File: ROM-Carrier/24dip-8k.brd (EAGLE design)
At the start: 33 x 26.7 mm, 7 parts

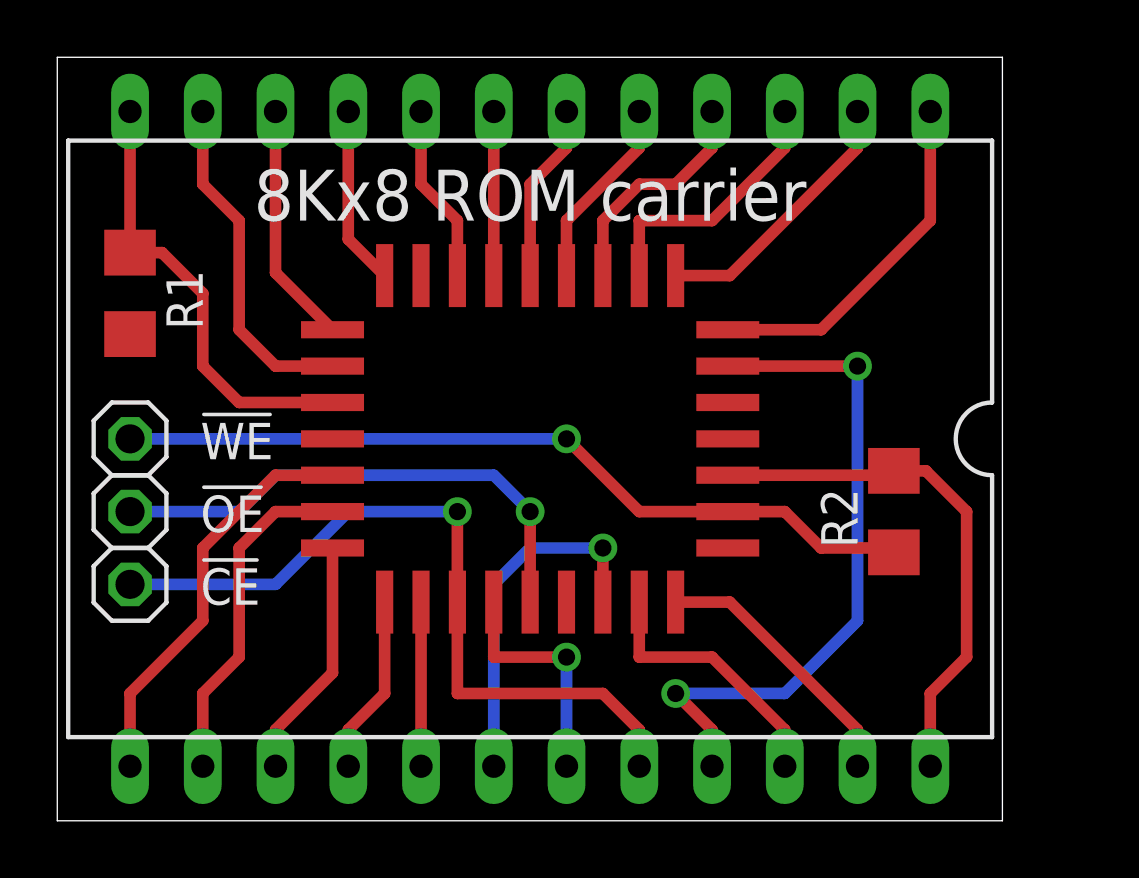
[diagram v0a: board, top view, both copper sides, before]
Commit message: fix carrier board (was 24-9, needed to be 24-6) removed unnecessary z80 support from 8080 sim
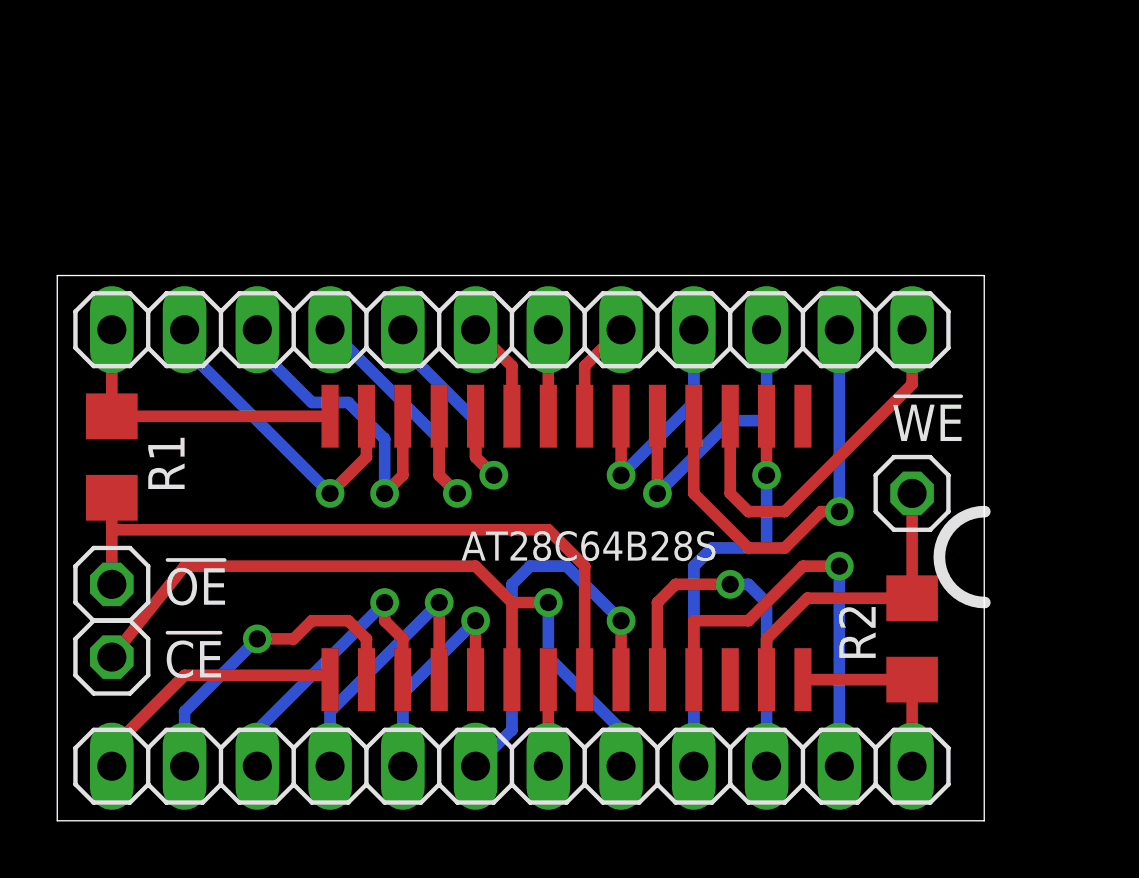
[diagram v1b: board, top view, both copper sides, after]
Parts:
- removed IC1: (no value), ic-package:DIL24-9
- added JP1, JP2: (no value), pinhead:1X12
- U$1: value AT28C64B32J -> AT28C64B28S; device eeprom:PLCCR32 -> eeprom:SO28W
- moved !WE 27.4 mm to (29.8, 11.4)
- moved R1 5.75 mm to (1.91, 12.7)
- moved R2 4.49 mm to (29.8, 6.35), turned to 270 degrees
- moved U$1 4.02 mm to (17.8, 9.53), turned to 180 degrees
- moved !CE 2.62 mm to (1.91, 5.71)
- moved !OE 2.62 mm to (1.91, 8.26)
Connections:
- net !CE: now also JP2.8, U$1.20; no longer IC1.20, U$1.23
- net +5V: now also JP2.12, U$1.28; no longer IC1.24, U$1.32
- net A0: now also JP1.8, U$1.10; no longer IC1.8, U$1.11
- net A1: now also JP1.7, U$1.9; no longer IC1.7, U$1.10
- net A10: now also JP2.7, U$1.21; no longer IC1.19, U$1.24
- net A11: now also JP2.6, U$1.23; no longer IC1.18, U$1.27
- net A12: now also JP2.9, U$1.2; no longer IC1.21, U$1.3
- net A2: now also JP1.6, U$1.8; no longer IC1.6, U$1.9
- net A3: now also JP1.5, U$1.7; no longer IC1.5, U$1.8
- net A4: now also JP1.4, U$1.6; no longer IC1.4, U$1.7
- net A5: now also JP1.3, U$1.5; no longer IC1.3, U$1.6
- net A6: now also JP1.2, U$1.4; no longer IC1.2, U$1.5
- net A7: now also JP1.1, U$1.3; no longer IC1.1, U$1.4
- net A8: now also JP2.11, U$1.25; no longer IC1.23, U$1.29
- net A9: now also JP2.10, U$1.24; no longer IC1.22, U$1.28
- net D0: now also JP1.9, U$1.11; no longer IC1.9, U$1.13
- net D1: now also JP1.10, U$1.12; no longer IC1.10, U$1.14
- net D2: now also JP1.11, U$1.13; no longer IC1.11, U$1.15
- net D3: now also JP2.1, U$1.15; no longer IC1.13, U$1.18
- net D4: now also JP2.2, U$1.16; no longer IC1.14, U$1.19
- net D5: now also JP2.3, U$1.17; no longer IC1.15, U$1.20
- net D6: now also JP2.4, U$1.18; no longer IC1.16, U$1.21
- net D7: now also JP2.5, U$1.19; no longer IC1.17, U$1.22
- net GND: now also JP1.12, U$1.14; no longer IC1.12, U$1.16
- net N$1: now also U$1.27; no longer U$1.31
- net N$2: now also U$1.22; no longer U$1.25
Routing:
- net N$1: track 28.3 -> 10.8 mm, vias 1 -> 0
- net +5V: track 18.4 -> 6.83 mm
- net A12: track 23.9 -> 14.4 mm, vias 2 -> 1
- net A6: track 9.47 -> 15.4 mm, vias 0 -> 1
- net N$2: track 18.2 -> 24.0 mm, vias 1 -> 0
- net A8: track 9.47 -> 14.9 mm, vias 0 -> 1
- net A10: track 8.27 -> 3.02 mm, vias 1 -> 0
- net GND: track 15.7 -> 10.6 mm
- net D3: track 14.3 -> 9.37 mm
- net D0: track 6.26 -> 10.5 mm, vias 0 -> 1
- net D6: track 6.26 -> 9.99 mm, vias 0 -> 1
- net A9: track 9.32 -> 12.7 mm, vias 0 -> 1
- net A2: track 6.26 -> 3.02 mm
- net A3: track 6.78 -> 3.55 mm
- net D1: track 8.44 -> 11.3 mm, vias 0 -> 1
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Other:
- board size 33 x 26.7 mm -> 32.4 x 19 mm
